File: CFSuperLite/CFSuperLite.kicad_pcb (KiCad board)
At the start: 2 copper layers, 99.9 x 99.9 mm, 24 parts, among them J1 IDE to CF adapter, J2 CF Adapter Power, J3 Bus_ISA_8bit, SW1 Options, U1 BIOS FLASH, U2 74HCT245, U3 ATF/GAL16V8x-15, U4 DS1315, Y1 32.768 KHz

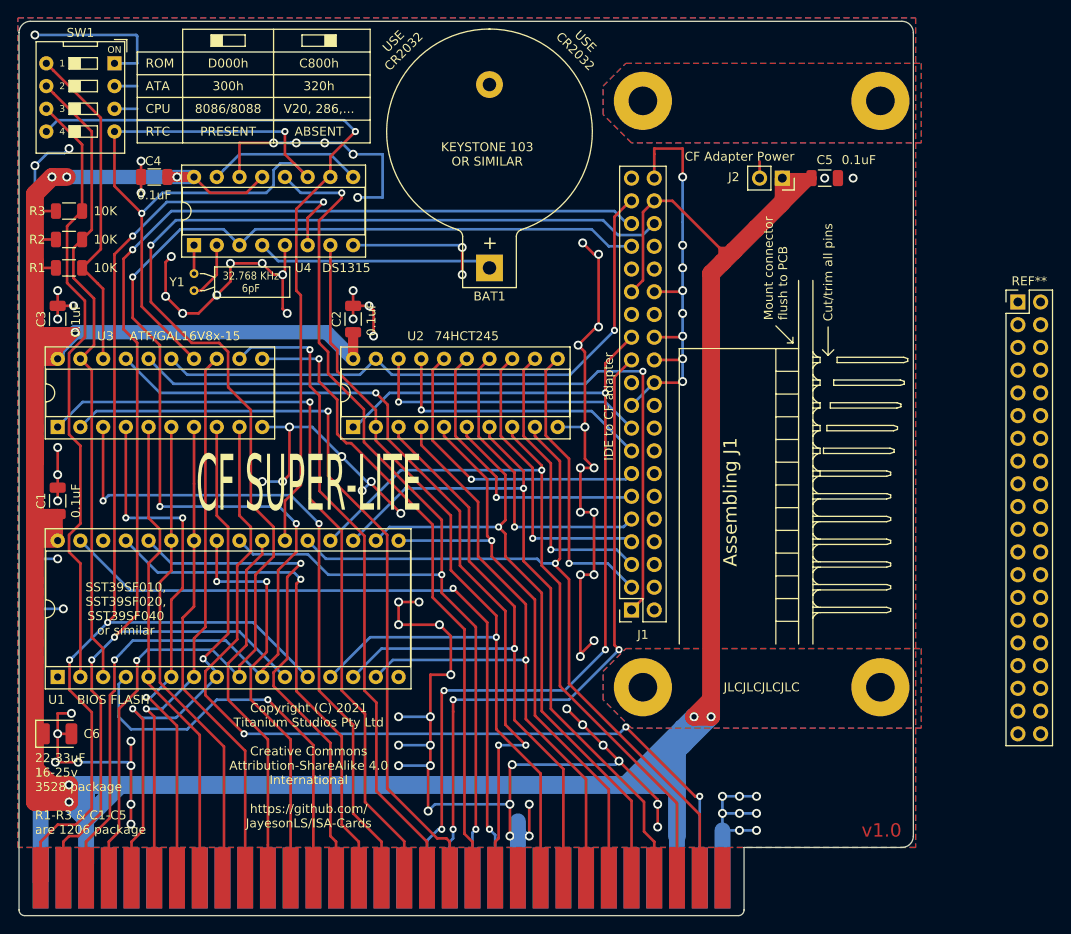
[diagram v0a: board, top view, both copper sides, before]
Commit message: CFSuperLite: Switch one tantalum to two smaller ones which are part of JLCPCB's basic part library.
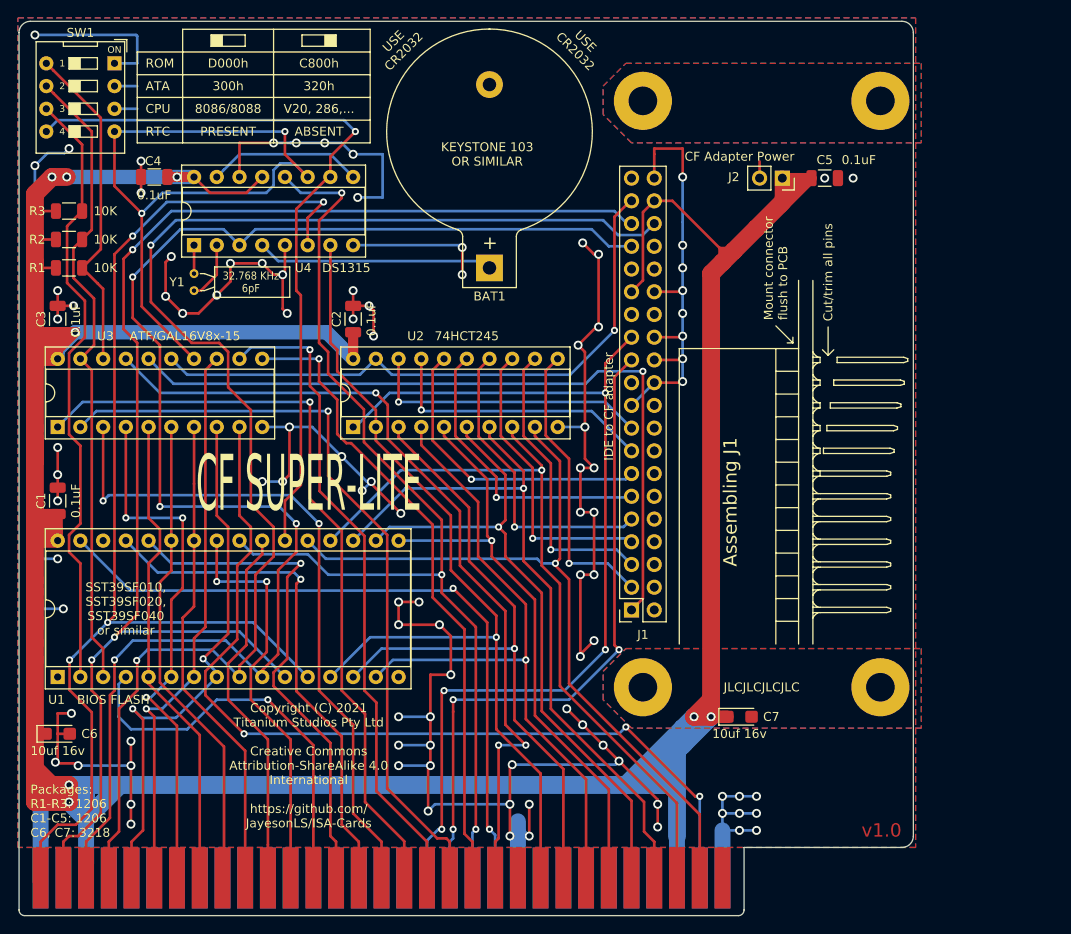
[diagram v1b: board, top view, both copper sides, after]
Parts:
- removed REF**: PinHeader_2x20_P2.54mm_Vertical, Connector_PinHeader_2.54mm:PinHeader_2x20_P2.54mm_Vertical
- added C7: 10uf 16v, Capacitor_Tantalum_SMD:CP_EIA-3216-18_Kemet-A, F.Cu at (177.2, 120.0)
- C6: value 22-44uF 16-25v -> 10uf 16v; footprint Capacitor_Tantalum_SMD:CP_EIA-3528-15_AVX-H -> Capacitor_Tantalum_SMD:CP_EIA-3216-18_Kemet-A
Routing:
- net VCC: track 460.4 -> 463.0 mm
- net GND: vias 101 -> 100
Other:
- board text added: "Packages: R1-R3: 1206 C1-C5: 1206 C6, C7: 3218"
- board text removed: "22-33uF 16-25v 3528 package"
- board text removed: "R1-R3 & C1-C5 are 1206 package"

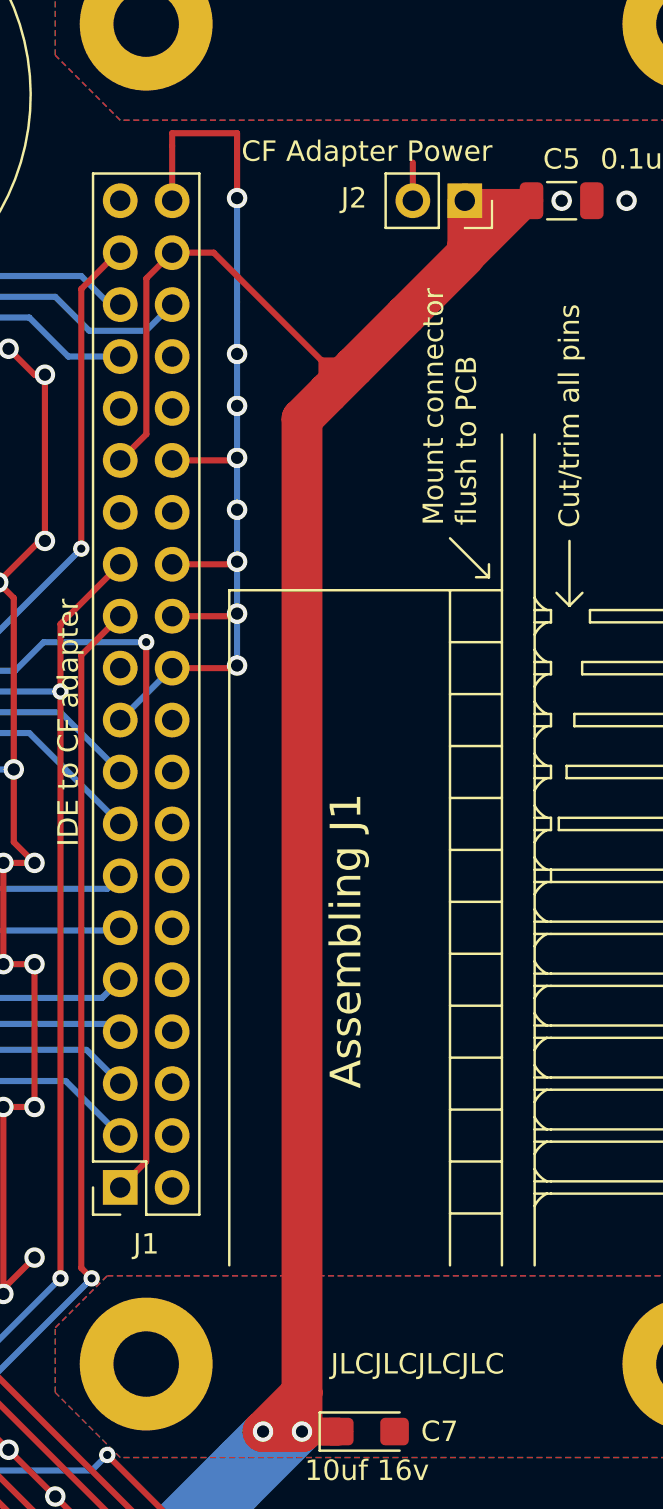
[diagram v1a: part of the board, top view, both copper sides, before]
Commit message: CFSuperLite: Duplicate J1 assembling instructions on rear side.
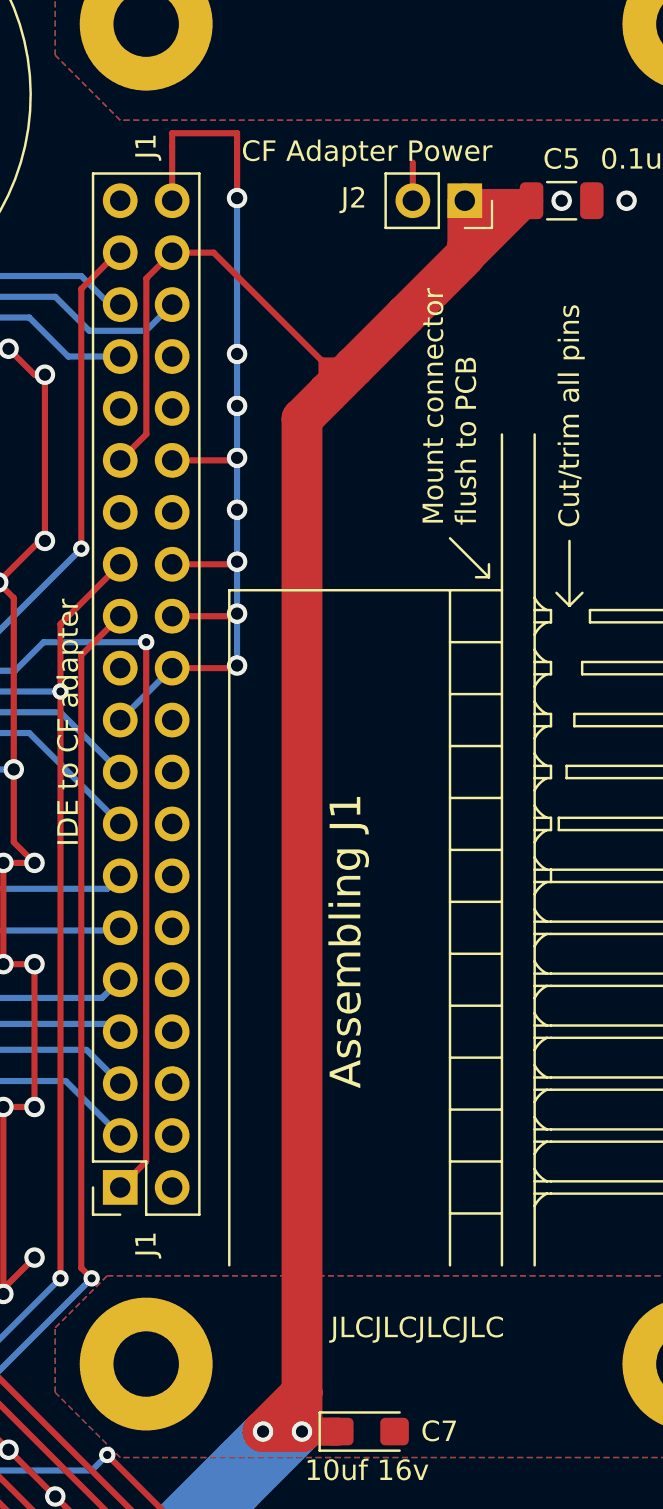
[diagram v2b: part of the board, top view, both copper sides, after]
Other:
- board text added: "J1"

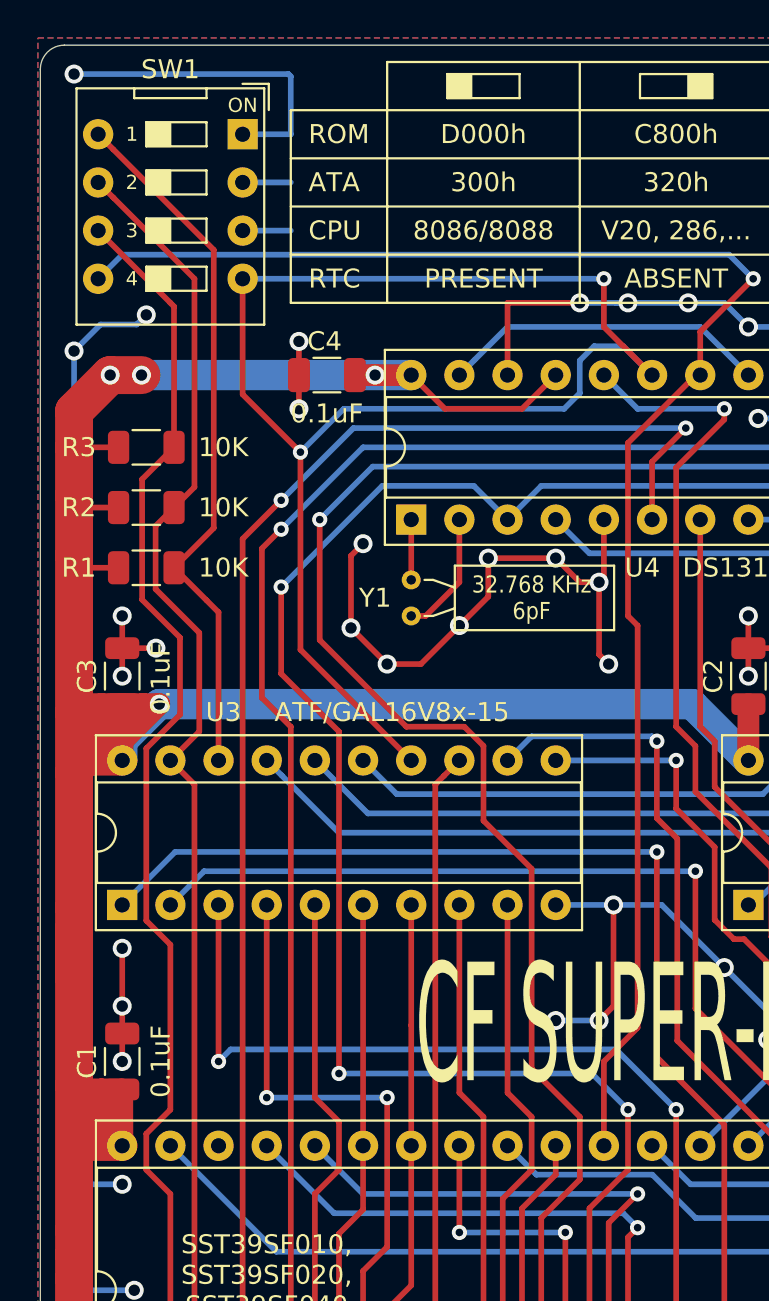
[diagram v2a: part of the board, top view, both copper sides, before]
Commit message: CFSuperLite: Add option to use 3-way DIP switch and 0 ohm resistor for assembly variation without RTC parts.
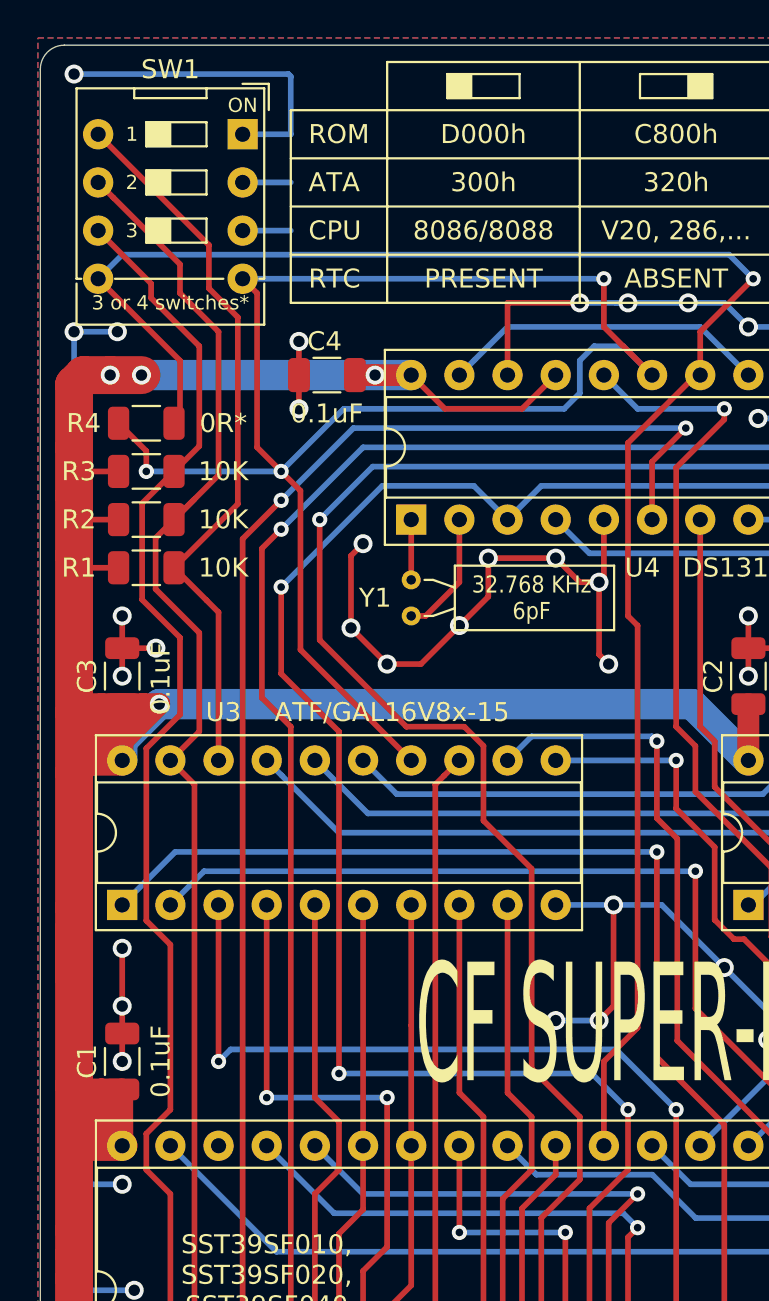
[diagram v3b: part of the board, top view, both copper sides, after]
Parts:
- added R4: 0R, Resistor_SMD:R_1206_3216Metric, F.Cu at (102.2, 62.2)
- moved R3 1.27 mm to (102.2, 64.8), turned to 180 degrees
- moved R2 0.64 mm to (102.2, 67.3), turned to 180 degrees
- turned R1 to 180 degrees
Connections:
- R1 pad 1: VCC -> ROM_ADDR_JUMPER
- R1 pad 2: ROM_ADDR_JUMPER -> VCC
- R2 pad 1: VCC -> ATA_ADDR_JUMPER
- R2 pad 2: ATA_ADDR_JUMPER -> VCC
- R3 pad 1: VCC -> V20_JUMPER
- R3 pad 2: V20_JUMPER -> VCC
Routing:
- net ~CE~_BIOS_DECODE: track 76.8 -> 88.5 mm, vias 2 -> 3
- net ~CE~_BIOS_THRU: track 85.1 -> 94.7 mm
- net ATA_ADDR_JUMPER: track 71.6 -> 74.2 mm
- net GND: track 501.1 -> 499.8 mm
- net V20_JUMPER: track 69.0 -> 70.1 mm
- net ROM_ADDR_JUMPER: track 37.4 -> 38.4 mm
- net VCC: track 463.0 -> 463.8 mm
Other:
- board text added: "* If RTC components are not fitted, a 3-way DIP switch may be used for for SW1 and a zero ohm resistor fitted to R4. Otherwise leave R4 unpopulated."
- board text added: "0R*"

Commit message: Update boards.
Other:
- board text added: "Created by Jayeson Lee-Steere https://github.com/ JayesonLS/ISA-Cards"
- board text removed: "Copyright (C) 2021 Titanium Studios Pty Ltd Creative Commons Attribution-ShareAlike 4.0 International https://github.com/ JayesonLS/ISA-Cards"
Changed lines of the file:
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@@
     (fp_line (start -8.95 10.3) (end -8.95 -2.7) (layer F.CrtYd) (width 0.05))
     (fp_line (start -8.95 -2.7) (end 1.35 -2.7) (layer F.CrtYd) (width 0.05))
-    (fp_text user on (at -5.365 -1.4975) (layer F.Fab)
-      (effects (font (size 0.8 0.8) (thickness 0.12)))
-    )
-    (fp_text user %R (at -7.62 -3.81 180) (layer F.Fab)
-      (effects (font (size 0.8 0.8) (thickness 0.12)))
-    )
-    (fp_text user 1 (at -5.842 0) (layer F.SilkS)
-      (effects (font (size 0.75 0.75) (thickness 0.15)))
-    )
-    (fp_text user 2 (at -5.842 2.54) (layer F.SilkS)
-      (effects (font (size 0.75 0.75) (thickness 0.15)))
-    )
-    (fp_text user 3 (at -5.842 5.08) (layer F.SilkS)
-      (effects (font (size 0.75 0.75) (thickness 0.15)))
-    )
-    (fp_text user ON (at 0 -1.524) (layer F.SilkS)
-      (effects (font (size 0.75 0.75) (thickness 0.15)))
-    )
     (fp_line (start 0.889 7.62) (end 1.14 7.62) (layer F.SilkS) (width 0.12))
     (fp_line (start -8.76 7.62) (end -8.509 7.62) (layer F.SilkS) (width 0.12))
@@
     (fp_line (start 1.14 7.874) (end 1.14 10.033) (layer F.SilkS) (width 0.12))
     (fp_line (start -8.76 7.874) (end -8.76 10.033) (layer F.SilkS) (width 0.12))
+    (fp_text user on (at -5.365 -1.4975) (layer F.Fab)
+      (effects (font (size 0.8 0.8) (thickness 0.12)))
+    )
+    (fp_text user %R (at -7.62 -3.81 180) (layer F.Fab)
+      (effects (font (size 0.8 0.8) (thickness 0.12)))
+    )
+    (fp_text user 1 (at -5.842 0) (layer F.SilkS)
+      (effects (font (size 0.75 0.75) (thickness 0.15)))
+    )
+    (fp_text user 2 (at -5.842 2.54) (layer F.SilkS)
+      (effects (font (size 0.75 0.75) (thickness 0.15)))
+    )
+    (fp_text user 3 (at -5.842 5.08) (layer F.SilkS)
+      (effects (font (size 0.75 0.75) (thickness 0.15)))
+    )
+    (fp_text user ON (at 0 -1.524) (layer F.SilkS)
+      (effects (font (size 0.75 0.75) (thickness 0.15)))
+    )
     (fp_text user "3 or 4 switches*" (at -3.81 8.89) (layer F.SilkS)
       (effects (font (size 0.75 0.75) (thickness 0.15)))
@@
     (fp_text value 0R (at 0 1.82) (layer F.Fab)
       (effects (font (size 1 1) (thickness 0.15)))
-    )
-    (fp_text user %R (at 0 0) (layer F.Fab)
-      (effects (font (size 0.8 0.8) (thickness 0.12)))
     )
     (fp_line (start -1.6 0.8) (end -1.6 -0.8) (layer F.Fab) (width 0.1))
@@
     (fp_line (start 2.28 -1.12) (end 2.28 1.12) (layer F.CrtYd) (width 0.05))
     (fp_line (start 2.28 1.12) (end -2.28 1.12) (layer F.CrtYd) (width 0.05))
+    (fp_text user %R (at 0 0) (layer F.Fab)
+      (effects (font (size 0.8 0.8) (thickness 0.12)))
+    )
     (pad 2 smd roundrect (at 1.4625 0) (size 1.125 1.75) (layers F.Cu F.Paste F.Mask) (roundrect_rratio 0.222222)
       (net 69 ~CE~_BIOS_THRU))
@@
     (effects (font (size 0.9 0.8) (thickness 0.15)))
   )
-  (gr_text "Copyright (C) 2021\nTitanium Studios Pty Ltd\n\nCreative Commons\nAttribution-ShareAlike 4.0\nInternational\n\nhttps://github.com/\nJayesonLS/ISA-Cards" (at 129.02 125.476) (layer F.SilkS)
+  (gr_text "Created by\nJayeson Lee-Steere\n\nhttps://github.com/\nJayesonLS/ISA-Cards" (at 129.02 125.476) (layer F.SilkS)
     (effects (font (size 1 1) (thickness 0.15)))
   )
